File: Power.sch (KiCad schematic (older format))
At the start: 35 parts, among them T5 Test_Point, T6 Test_Point, T7 Test_Point, U4 MP4570GF, U5 AP65251, U6 AZ1117-3.3

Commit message: Replaced the 16V 1μF with a 25V-Version to use them on the 12V-Rail
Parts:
- C20, C21, C8: Buy https://www.digikey.com/product-detail/en/samsung-electro-m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 -> https://www.digikey.com/product-detail/en/taiyo-yuden/TMK21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
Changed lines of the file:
@@
 F 2 "Capacitor_SMD:C_0805_2012Metric" H 1175 1100 50  0001 C CNN
 F 3 "~" H 1175 1100 50  0001 C CNN
-F 4 "https://www.digikey.com/product-detail/en/samsung-electro-mechanics/CL21B105KOFNNNE/1276-1026-1-ND/3889112" H 1175 1100 50  0001 C CNN "Buy"
+F 4 "https://www.digikey.com/product-detail/en/taiyo-yuden/TMK212B7105MG-T/587-5595-1-ND/7067270" H 1175 1100 50  0001 C CNN "Buy"
 	1    1175 1100
 	0    1    1    0
@@
 F 2 "Capacitor_SMD:C_0805_2012Metric" H 9163 1725 50  0001 C CNN
 F 3 "~" H 9125 1875 50  0001 C CNN
-F 4 "https://www.digikey.com/product-detail/en/samsung-electro-mechanics/CL21B105KOFNNNE/1276-1026-1-ND/3889112" H 9125 1875 50  0001 C CNN "Buy"
+F 4 "https://www.digikey.com/product-detail/en/taiyo-yuden/TMK212B7105MG-T/587-5595-1-ND/7067270" H 9125 1875 50  0001 C CNN "Buy"
 	1    9125 1875
 	1    0    0    -1
@@
 F 2 "Capacitor_SMD:C_0805_2012Metric" H 10488 1725 50  0001 C CNN
 F 3 "~" H 10450 1875 50  0001 C CNN
-F 4 "https://www.digikey.com/product-detail/en/samsung-electro-mechanics/CL21B105KOFNNNE/1276-1026-1-ND/3889112" H 10450 1875 50  0001 C CNN "Buy"
+F 4 "https://www.digikey.com/product-detail/en/taiyo-yuden/TMK212B7105MG-T/587-5595-1-ND/7067270" H 10450 1875 50  0001 C CNN "Buy"
 	1    10450 1875
 	1    0    0    -1

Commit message: Replaced the Digikey-Field with a Buy-Field
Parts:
- C? (x2): Buy (none) -> https://www.digikey.com/product-detail/en/yageo/CC0603JRNPO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; Digikey https://www.digikey.com/product-detail/en/yageo/CC0603JRNPO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 -> (none)
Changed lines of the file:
@@
 F 2 "Capacitor_SMD:C_0603_1608Metric" H 7050 1825 50  0001 C CNN
 F 3 "~" H 7050 1825 50  0001 C CNN
-F 4 "https://www.digikey.com/product-detail/en/yageo/CC0603JRNPO9BN150/311-1060-1-ND/302970" H 7050 1825 50  0001 C CNN "Digikey"
+F 4 "https://www.digikey.com/product-detail/en/yageo/CC0603JRNPO9BN150/311-1060-1-ND/302970" H 7050 1825 50  0001 C CNN "Buy"
 	1    7050 1825
 	1    0    0    -1
@@
 F 2 "Capacitor_SMD:C_0603_1608Metric" H 7275 1825 50  0001 C CNN
 F 3 "~" H 7275 1825 50  0001 C CNN
-F 4 "https://www.digikey.com/product-detail/en/yageo/CC0603JRNPO9BN150/311-1060-1-ND/302970" H 7275 1825 50  0001 C CNN "Digikey"
+F 4 "https://www.digikey.com/product-detail/en/yageo/CC0603JRNPO9BN150/311-1060-1-ND/302970" H 7275 1825 50  0001 C CNN "Buy"
 	1    7275 1825
 	1    0    0    -1

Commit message: Created 6.6x6.6mm Elec-Footprint and added it to Schematic and Library-Table
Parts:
- C12, C14, C18: footprint (none) -> CP_Elec:CP_Elec_6.6x6.6mm_P2.25mm_D6.3mm
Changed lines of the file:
@@
 F 0 "C12" H 3785 2170 50  0000 L CNN
 F 1 "47μF" H 3785 2020 50  0000 L CNN
-F 2 "" H 3775 2100 50  0001 C CNN
+F 2 "CP_Elec:CP_Elec_6.6x6.6mm_P2.25mm_D6.3mm" H 3775 2100 50  0001 C CNN
 F 3 "" H 3775 2100 50  0001 C CNN
 F 4 "https://www.digikey.com/product-detail/en/rubycon/25TXV47M6.3X8/1189-2118-1-ND/3987037" H 3775 2100 50  0001 C CNN "Buy"
@@
 F 0 "C14" H 4685 1620 50  0000 L CNN
 F 1 "47μF" H 4685 1470 50  0000 L CNN
-F 2 "" H 4675 1550 50  0001 C CNN
+F 2 "CP_Elec:CP_Elec_6.6x6.6mm_P2.25mm_D6.3mm" H 4675 1550 50  0001 C CNN
 F 3 "" H 4675 1550 50  0001 C CNN
 F 4 "https://www.digikey.com/product-detail/en/rubycon/25TXV47M6.3X8/1189-2118-1-ND/3987037" H 4675 1550 50  0001 C CNN "Buy"
@@
 F 0 "C18" H 7975 1925 50  0000 L CNN
 F 1 "47μF" H 7975 1725 50  0000 L CNN
-F 2 "" H 7988 1675 50  0001 C CNN
+F 2 "CP_Elec:CP_Elec_6.6x6.6mm_P2.25mm_D6.3mm" H 7988 1675 50  0001 C CNN
 F 3 "" H 7950 1825 50  0001 C CNN
 F 4 "https://www.digikey.com/product-detail/en/rubycon/25TXV47M6.3X8/1189-2118-1-ND/3987037" H 7950 1825 50  0001 C CNN "Buy"

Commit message: Created the Footprint for the 12V-Buckinductor and added it to the project
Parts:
- C12, C14, C18: footprint CP_Elec:CP_Elec_6.6x6.6mm_P2.25mm_D6.3mm -> CP_Elec:CP_Elec_6.6x6.6mm_P4.5mm_D6.3mm
- C9: footprint (none) -> CP_Elec:CP_Elec_8.3x8.3mm_P6.5mm_D8mm
- L1: footprint (none) -> I_SMD:I_SMD_Bourne_12.7x12.7mm
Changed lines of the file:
@@
 F 0 "C9" H 1835 920 50  0000 L CNN
 F 1 "47μF" H 1835 770 50  0000 L CNN
-F 2 "" H 1825 850 50  0001 C CNN
+F 2 "CP_Elec:CP_Elec_8.3x8.3mm_P6.5mm_D8mm" H 1825 850 50  0001 C CNN
 F 3 "" H 1825 850 50  0001 C CNN
 F 4 "https://www.digikey.com/product-detail/en/panasonic-electronic-components/EEE-TG1J470UP/PCE4093CT-ND/817764" H 1825 850 50  0001 C CNN "Buy"
@@
 F 0 "L1" V 2575 1900 50  0000 C CNN
 F 1 "22μH" V 2700 1900 50  0000 C CNN
-F 2 "" H 2625 1900 50  0001 C CNN
+F 2 "I_SMD:I_SMD_Bourne_12.7x12.7mm" H 2625 1900 50  0001 C CNN
 F 3 "" H 2625 1900 50  0001 C CNN
 F 4 "https://www.digikey.com/product-detail/en/bourns-inc/SRR1208-220ML/SRR1208-220MLCT-ND/2353019" V 2625 1900 50  0001 C CNN "Buy"
@@
 F 0 "C12" H 3785 2170 50  0000 L CNN
 F 1 "47μF" H 3785 2020 50  0000 L CNN
-F 2 "CP_Elec:CP_Elec_6.6x6.6mm_P2.25mm_D6.3mm" H 3775 2100 50  0001 C CNN
+F 2 "CP_Elec:CP_Elec_6.6x6.6mm_P4.5mm_D6.3mm" H 3775 2100 50  0001 C CNN
 F 3 "" H 3775 2100 50  0001 C CNN
 F 4 "https://www.digikey.com/product-detail/en/rubycon/25TXV47M6.3X8/1189-2118-1-ND/3987037" H 3775 2100 50  0001 C CNN "Buy"
@@
 F 0 "C14" H 4685 1620 50  0000 L CNN
 F 1 "47μF" H 4685 1470 50  0000 L CNN
-F 2 "CP_Elec:CP_Elec_6.6x6.6mm_P2.25mm_D6.3mm" H 4675 1550 50  0001 C CNN
+F 2 "CP_Elec:CP_Elec_6.6x6.6mm_P4.5mm_D6.3mm" H 4675 1550 50  0001 C CNN
 F 3 "" H 4675 1550 50  0001 C CNN
 F 4 "https://www.digikey.com/product-detail/en/rubycon/25TXV47M6.3X8/1189-2118-1-ND/3987037" H 4675 1550 50  0001 C CNN "Buy"
@@
 F 0 "C18" H 7975 1925 50  0000 L CNN
 F 1 "47μF" H 7975 1725 50  0000 L CNN
-F 2 "CP_Elec:CP_Elec_6.6x6.6mm_P2.25mm_D6.3mm" H 7988 1675 50  0001 C CNN
+F 2 "CP_Elec:CP_Elec_6.6x6.6mm_P4.5mm_D6.3mm" H 7988 1675 50  0001 C CNN
 F 3 "" H 7950 1825 50  0001 C CNN
 F 4 "https://www.digikey.com/product-detail/en/rubycon/25TXV47M6.3X8/1189-2118-1-ND/3987037" H 7950 1825 50  0001 C CNN "Buy"

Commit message: Associated the Footprint for the 5V-Buckinductor
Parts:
- L2: footprint (none) -> Inductor_SMD:L_Taiyo-Yuden_NR-80xx
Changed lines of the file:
@@
 F 0 "L2" V 6625 1675 50  0000 C CNN
 F 1 "22μH" V 6500 1675 50  0000 C CNN
-F 2 "" H 6550 1675 50  0001 C CNN
+F 2 "Inductor_SMD:L_Taiyo-Yuden_NR-80xx" H 6550 1675 50  0001 C CNN
 F 3 "" H 6550 1675 50  0001 C CNN
 F 4 "https://www.digikey.com/product-detail/en/taiyo-yuden/NR8040T220M/587-2002-1-ND/1739114" V 6550 1675 50  0001 C CNN "Buy"

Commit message: Associated the TestPoints with their Footprints
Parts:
- T5: footprint (none) -> TestPoint:TestPoint_Pad_D4.0mm
- T6: footprint (none) -> TestPoint:TestPoint_Pad_D3.0mm
- T7: footprint (none) -> TestPoint:TestPoint_Pad_D2.0mm
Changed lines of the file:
@@
 F 0 "T7" H 10400 1875 50  0000 L CNN
 F 1 "Test_Point" H 10508 1704 50  0001 L CNN
-F 2 "" H 10650 1675 50  0001 C CNN
+F 2 "TestPoint:TestPoint_Pad_D2.0mm" H 10650 1675 50  0001 C CNN
 F 3 "~" H 10650 1675 50  0001 C CNN
 	1    10450 1675
@@
 F 0 "T6" H 7900 1875 50  0000 L CNN
 F 1 "Test_Point" H 8008 1704 50  0001 L CNN
-F 2 "" H 8150 1675 50  0001 C CNN
+F 2 "TestPoint:TestPoint_Pad_D3.0mm" H 8150 1675 50  0001 C CNN
 F 3 "~" H 8150 1675 50  0001 C CNN
 	1    7950 1675
@@
 F 0 "T5" H 3425 2100 50  0000 L CNN
 F 1 "Test_Point" H 3533 1929 50  0001 L CNN
-F 2 "" H 3675 1900 50  0001 C CNN
+F 2 "TestPoint:TestPoint_Pad_D4.0mm" H 3675 1900 50  0001 C CNN
 F 3 "~" H 3675 1900 50  0001 C CNN
 	1    3475 1900

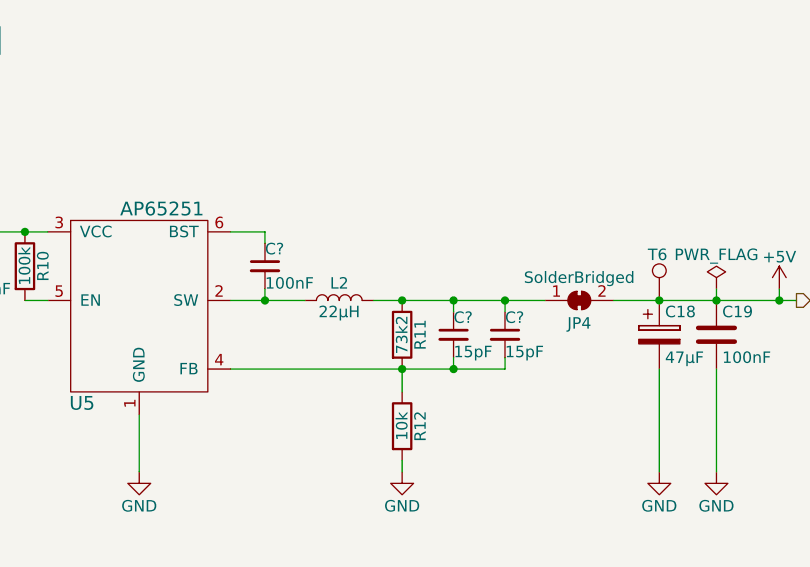
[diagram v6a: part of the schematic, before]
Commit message: Associated the SolderBrigdes with their Footprints
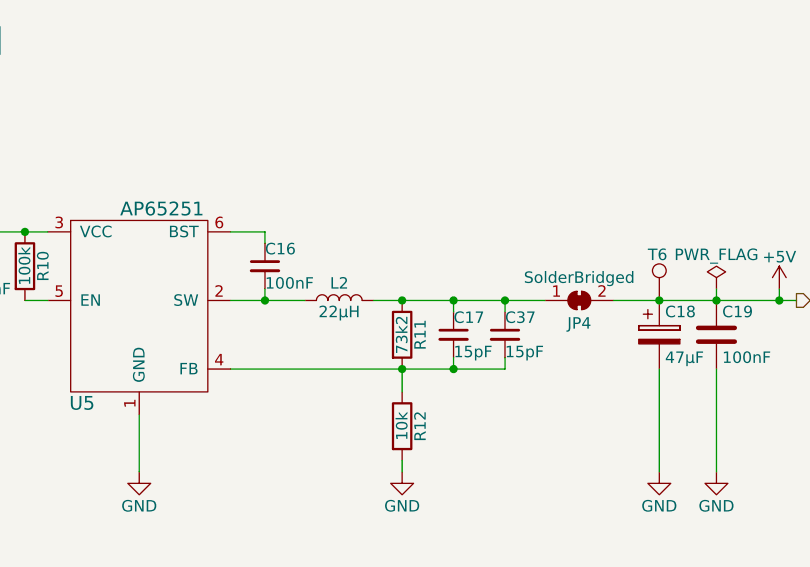
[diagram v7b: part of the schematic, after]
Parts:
- JP3, JP4, JP5: footprint (none) -> Jumper:SolderJumper-2_P1.3mm_Bridged_Pad1.0x1.5mm
- gave numbers to parts that had none: 3
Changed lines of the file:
@@
 F 0 "JP5" H 10125 1575 50  0000 C CNN
 F 1 "SolderBridged" H 10125 1775 50  0000 C CNN
-F 2 "" H 10125 1675 50  0001 C CNN
+F 2 "Jumper:SolderJumper-2_P1.3mm_Bridged_Pad1.0x1.5mm" H 10125 1675 50  0001 C CNN
 F 3 "~" H 10125 1675 50  0001 C CNN
 	1    10125 1675
@@
 F 0 "JP4" H 7600 1575 50  0000 C CNN
 F 1 "SolderBridged" H 7600 1775 50  0000 C CNN
-F 2 "" H 7600 1675 50  0001 C CNN
+F 2 "Jumper:SolderJumper-2_P1.3mm_Bridged_Pad1.0x1.5mm" H 7600 1675 50  0001 C CNN
 F 3 "~" H 7600 1675 50  0001 C CNN
 	1    7600 1675
@@
 F 0 "JP3" H 3125 1800 50  0000 C CNN
 F 1 "SolderBridged" H 3125 2000 50  0000 C CNN
-F 2 "" H 3125 1900 50  0001 C CNN
+F 2 "Jumper:SolderJumper-2_P1.3mm_Bridged_Pad1.0x1.5mm" H 3125 1900 50  0001 C CNN
 F 3 "~" H 3125 1900 50  0001 C CNN
 	1    3125 1900
@@
 	6075 1675 6225 1675
 $Comp
-L Device:C_Small C?
+L Device:C_Small C16
 U 1 1 5B03381C
 P 6225 1525
-F 0 "C?" H 6225 1600 50  0000 L CNN
+F 0 "C16" H 6225 1600 50  0000 L CNN
 F 1 "100nF" H 6225 1450 50  0000 L CNN
 F 2 "Capacitor_SMD:C_0805_2012Metric" H 6225 1525 50  0001 C CNN
@@
 Connection ~ 6825 1675
 $Comp
-L Device:C_Small C?
+L Device:C_Small C17
 U 1 1 5B03D3DF
 P 7050 1825
-F 0 "C?" H 7050 1900 50  0000 L CNN
+F 0 "C17" H 7050 1900 50  0000 L CNN
 F 1 "15pF" H 7050 1750 50  0000 L CNN
 F 2 "Capacitor_SMD:C_0603_1608Metric" H 7050 1825 50  0001 C CNN
@@
 $EndComp
 $Comp
-L Device:C_Small C?
+L Device:C_Small C37
 U 1 1 5B03D669
 P 7275 1825
-F 0 "C?" H 7275 1900 50  0000 L CNN
+F 0 "C37" H 7275 1900 50  0000 L CNN
 F 1 "15pF" H 7275 1750 50  0000 L CNN
 F 2 "Capacitor_SMD:C_0603_1608Metric" H 7275 1825 50  0001 C CNN

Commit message: Created the MP4570GF-Footprint and associated it
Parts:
- U4: footprint Package_SO:HTSSOP-20-1EP_4.4x6.5mm_P0.65mm_EP3.4x6.5mm_ThermalVias -> HTSSOP:HTSSOP-20_4.3x6.4mm_EP3.2x4.4mm_P0.65mm_ThermalPad
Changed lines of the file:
@@
 F 0 "U4" H 2025 2100 60  0000 C CNN
 F 1 "MP4570GF" H 1625 2900 60  0000 C CNN
-F 2 "Package_SO:HTSSOP-20-1EP_4.4x6.5mm_P0.65mm_EP3.4x6.5mm_ThermalVias" H 475 2900 60  0001 C CNN
+F 2 "HTSSOP:HTSSOP-20_4.3x6.4mm_EP3.2x4.4mm_P0.65mm_ThermalPad" H 475 2900 60  0001 C CNN
 F 3 "" H 475 2900 60  0001 C CNN
 F 4 "https://www.digikey.com/product-detail/en/monolithic-power-systems-inc/MP4570GF/1589-1406-ND/5299163" H 1625 2500 50  0001 C CNN "Buy"
